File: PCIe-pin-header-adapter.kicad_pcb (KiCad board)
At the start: 2 copper layers, 208.2 x 40.9 mm, 7 parts, among them J1 Conn_01x40_Male, J2 Conn_01x40_Male, J3 Conn_01x02_Male, J4 Connector_PCIe_x16, J5 Conn_01x40_Male, J6 Conn_01x40_Male, J7 Conn_01x02_Male

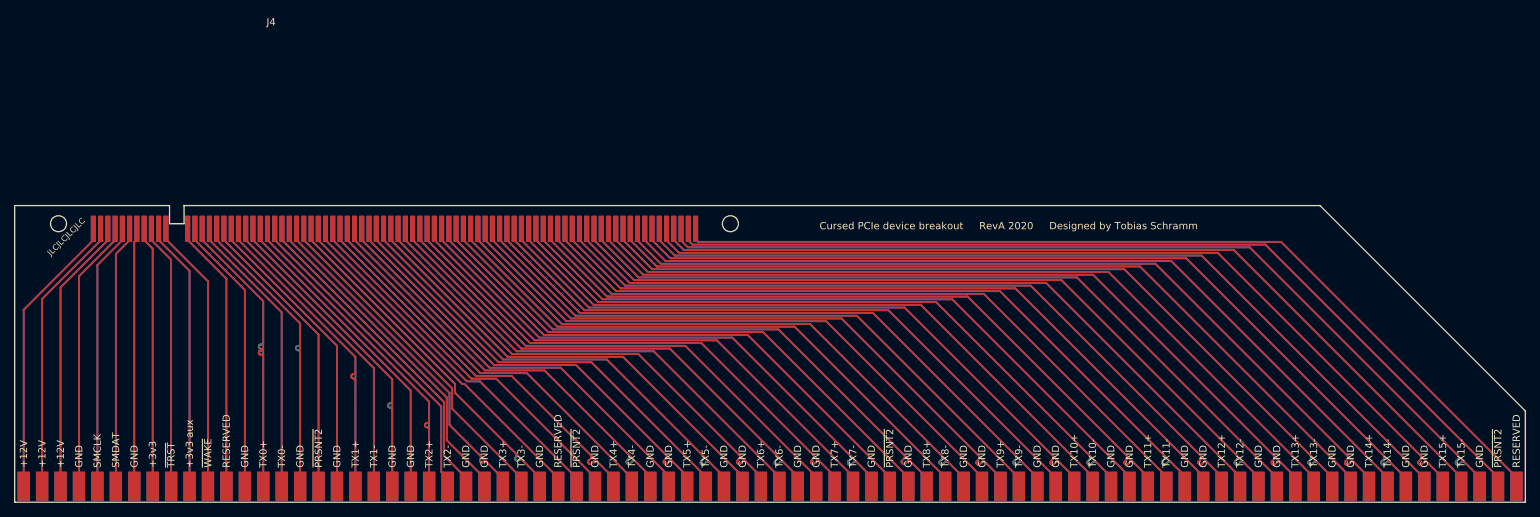
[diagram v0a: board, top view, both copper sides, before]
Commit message: Deepen PCIe x16 slot cutout
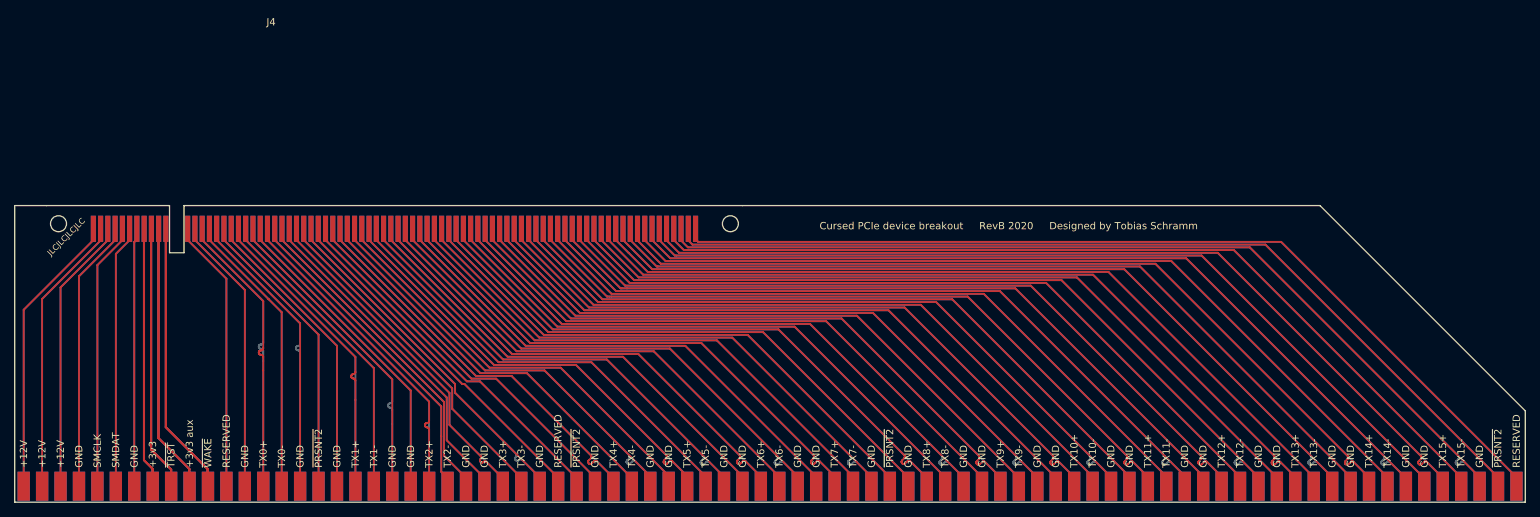
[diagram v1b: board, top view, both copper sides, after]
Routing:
- net Net-(J1-Pad33): track 35.9 -> 74.7 mm
- net Net-(J1-Pad30): track 37.9 -> 75.8 mm
- net Net-(J1-Pad31): track 37.2 -> 74.5 mm
- net Net-(J1-Pad32): track 36.4 -> 73.3 mm
- net Net-(J4-PadB12): track 39.2 -> 42.3 mm
- net Net-(J1-Pad29): track 39.2 -> 42.3 mm
- net Net-(J4-PadB16): track 40.9 -> 42.4 mm
- net Net-(J4-PadB15): track 39.7 -> 41.2 mm
- net Net-(J4-PadB14): track 39.7 -> 41.2 mm
- net Net-(J4-PadB13): track 38.3 -> 39.9 mm
- net Net-(J1-Pad28): track 38.3 -> 39.9 mm
- net Net-(J1-Pad27): track 39.7 -> 41.2 mm
- net Net-(J1-Pad26): track 39.7 -> 41.2 mm
- net Net-(J1-Pad25): track 40.2 -> 41.8 mm
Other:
- board text added: "Cursed PCIe device breakout RevB 2020 Designed by Tobias Schramm"
- board text removed: "Cursed PCIe device breakout RevA 2020 Designed by Tobias Schramm"
